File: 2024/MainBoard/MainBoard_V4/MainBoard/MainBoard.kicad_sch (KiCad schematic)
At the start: 15 parts, among them J1 Raspberry_Pi_2_3, SW1 SW_MEC_5E, U1 STM32F446RETx, Y1 CSTNE16M0V530000R0

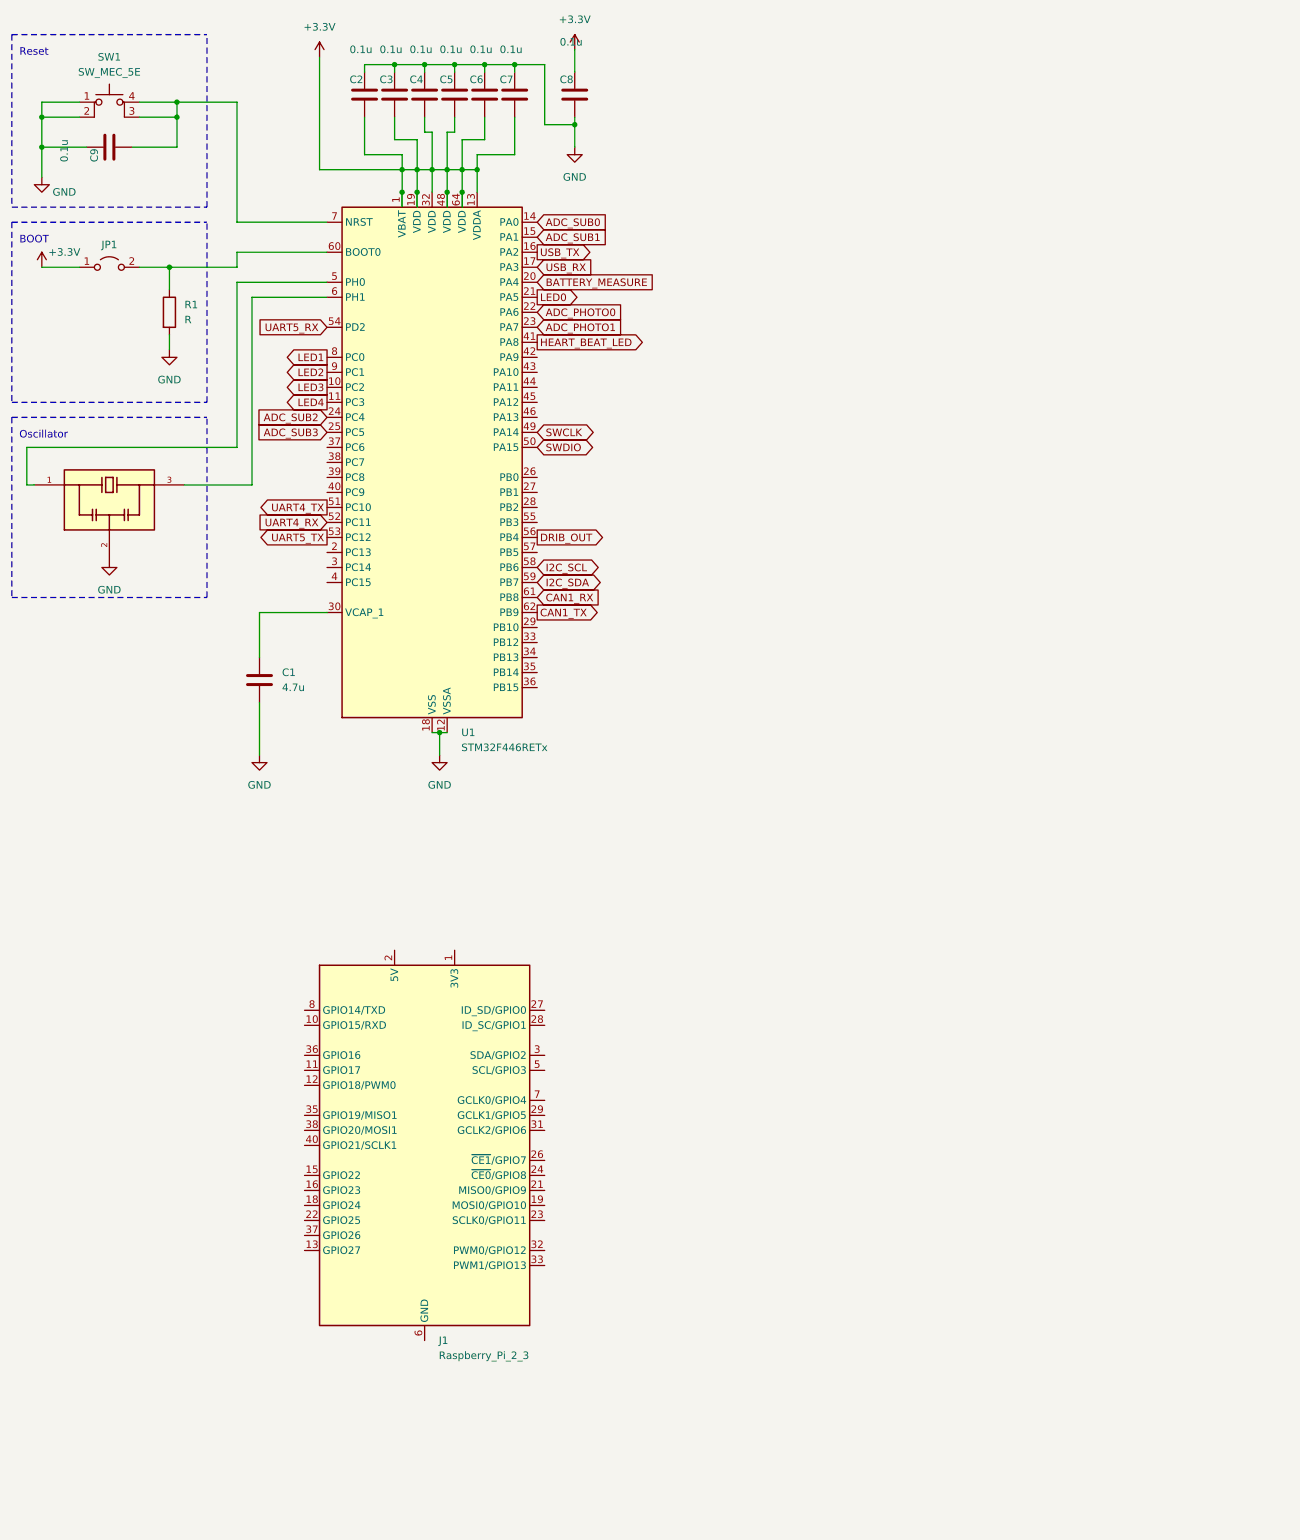
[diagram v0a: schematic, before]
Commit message: ✨ラズパイ周りとUSBシリアル変換周りの回路図を描いた
 USBを刺した時にラズパイが5Vで起動しないようにしないといけない?
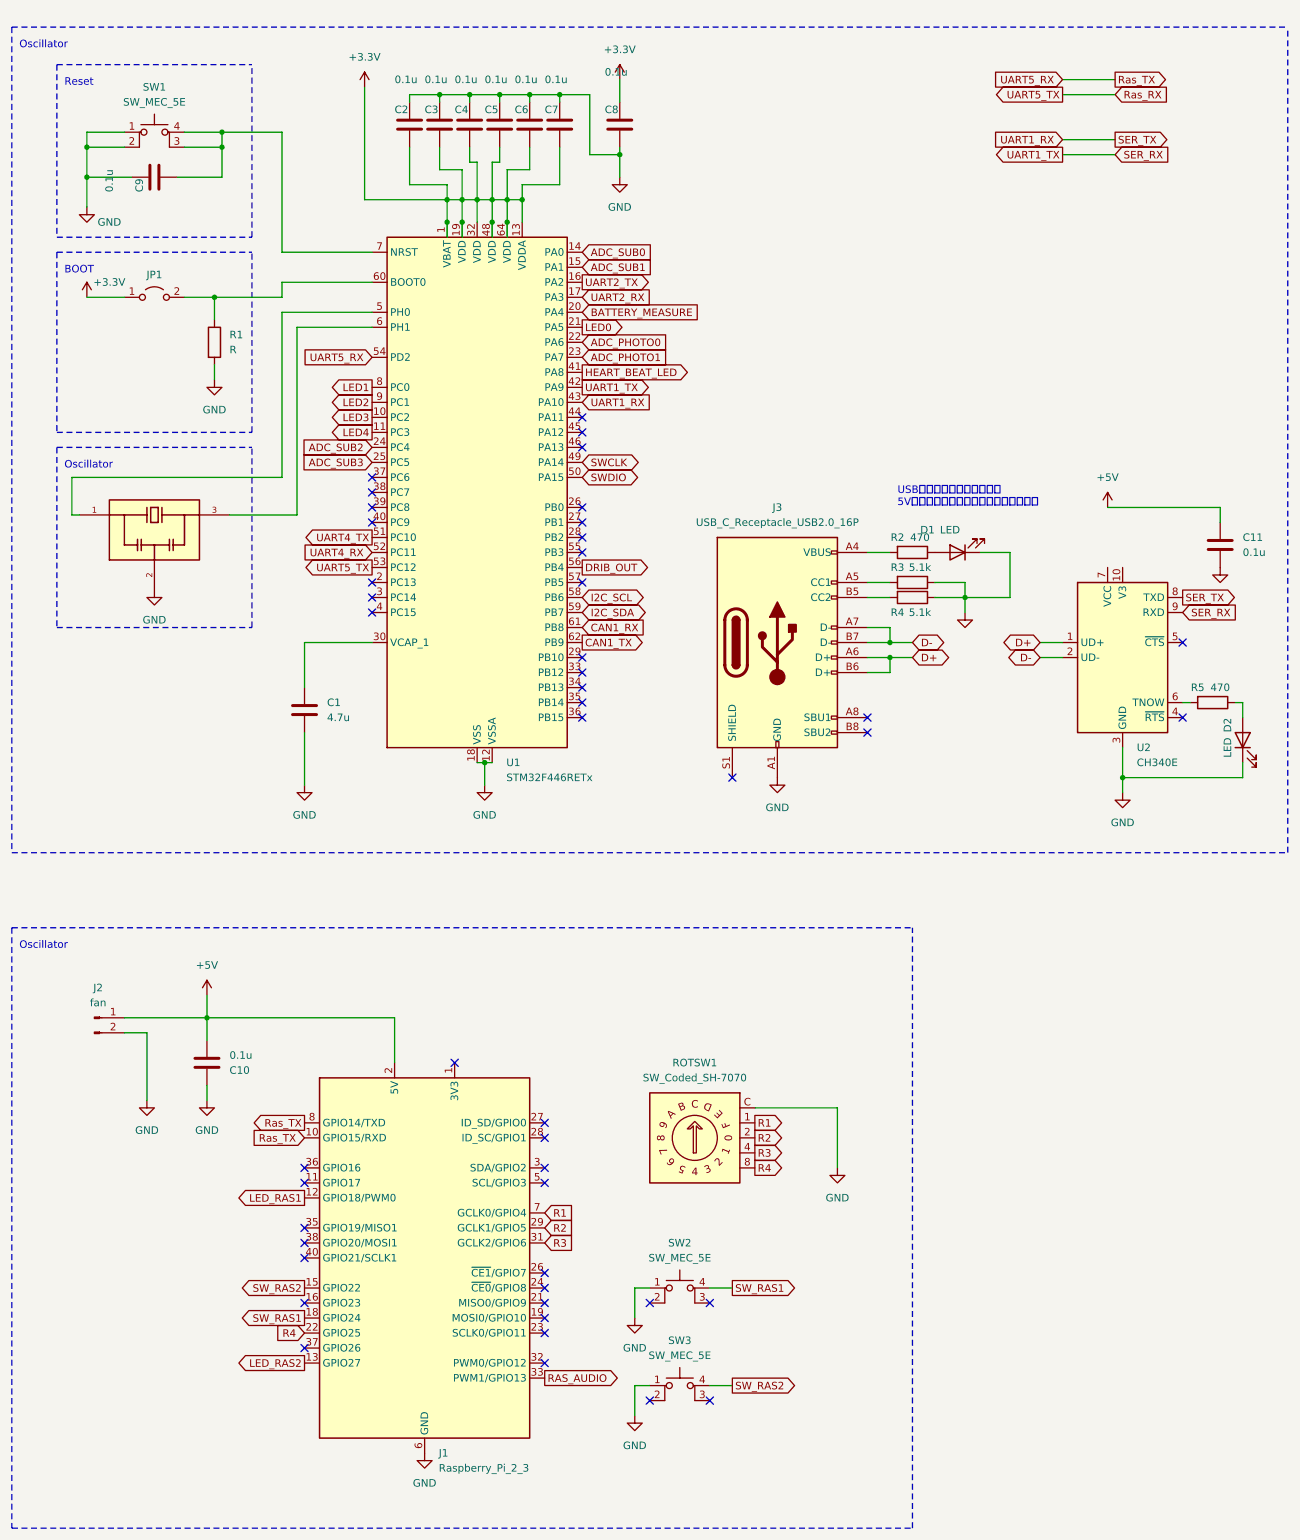
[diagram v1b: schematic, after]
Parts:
- added C10, C11: 0.1u, Capacitor_SMD:C_0504_1310Metric_Pad0.83x1.28mm_HandSolder, symbol Device:C
- added D1, D2: LED, LED_SMD:LED_0603_1608Metric_Pad1.05x0.95mm_HandSolder, symbol Device:LED
- added J2: fan, Resistor_SMD:R_2816_7142Metric_Pad3.20x4.45mm_HandSolder, symbol Connector:Conn_01x02_Pin
- added J3: USB_C_Receptacle_USB2.0_16P, Connector_USB:USB_C_Receptacle_GCT_USB4105-xx-A_16P_TopMnt_Horizontal, symbol Connector:USB_C_Receptacle_USB2.0_16P
- added R2, R5: 470, Resistor_SMD:R_0603_1608Metric_Pad0.98x0.95mm_HandSolder, symbol Device:R
- added R3, R4: 5.1k, Resistor_SMD:R_0603_1608Metric_Pad0.98x0.95mm_HandSolder, symbol Device:R
- added ROTSW1: SW_Coded_SH-7070, symbol Switch:SW_Coded_SH-7070
- added SW2, SW3: SW_MEC_5E, Button_Switch_THT:SW_PUSH_6mm, symbol Switch:SW_MEC_5E
- added U2: CH340E, Package_SO:MSOP-10_3x3mm_P0.5mm, symbol Interface_USB:CH340E
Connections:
- net UART5_RX is gone; now on net Ras_TX: U1.54 (PD2)
- net GND: now also J1.14 (GND), J1.20 (GND), J1.25 (GND), J1.30 (GND), J1.34 (GND), J1.39 (GND), J1.6 (GND), J1.9 (GND), C10.2, C11.2, D1.1 (K), D2.1 (K), J2.2 (Pin_2), J3.A1 (GND), J3.A12 (GND), J3.B1 (GND), J3.B12 (GND), R3.1, R4.1, ROTSW1.C, SW2.1, SW3.1, U2.3 (GND)
- net Ras_TX: now reaches J1.10 (GPIO15/RXD)
- net Ras_TX: now also J1.8 (GPIO14/TXD)
- net LED_RAS1: now reaches J1.12 (GPIO18/PWM0)
- net LED_RAS2: now reaches J1.13 (GPIO27)
- net SW_RAS2: now reaches J1.15 (GPIO22)
- net SW_RAS2: now also SW3.4 (A)
- net SW_RAS1: now reaches J1.18 (GPIO24)
- net SW_RAS1: now also SW2.4 (A)
- net +5V: now reaches J1.2 (5V), J1.4 (5V)
- net +5V: now also C10.1, C11.1, J2.1 (Pin_1)
- net R4: now reaches J1.22 (GPIO25)
- net R4: now also ROTSW1.8
- net R2: now reaches J1.29 (GCLK1/GPIO5)
- net R2: now also ROTSW1.2
- net R3: now reaches J1.31 (GCLK2/GPIO6)
- net R3: now also ROTSW1.4
- net RAS_AUDIO: now reaches J1.33 (PWM1/GPIO13)
- net R1: now reaches J1.7 (GCLK0/GPIO4)
- net R1: now also ROTSW1.1
- net SER_RX: now reaches U1.42 (PA9)
- net SER_RX: now also U2.9 (RXD)
- net SER_TX: now reaches U1.43 (PA10)
- net SER_TX: now also U2.8 (TXD)
- net UART5_TX renamed Ras_RX
- net USB_RX renamed UART2_RX
- net USB_TX renamed UART2_TX
- new net: J3.B5 (CC2), R4.2
- new net: J3.A5 (CC1), R3.2
- new net: R5.2, U2.6 (TNOW)
- new net: D2.2 (A), R5.1
- new net: D1.2 (A), R2.1
- new net: J3.A4 (VBUS), J3.A9 (VBUS), J3.B4 (VBUS), J3.B9 (VBUS), R2.2
- new net D+: J3.A6 (D+), J3.B6 (D+), U2.1 (UD+)
- new net D-: J3.A7 (D-), J3.B7 (D-), U2.2 (UD-)
- no-connect marks 0 -> 47
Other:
- note added: "USBを刺した時にラズパイが 5Vで起動しないようにしないといけない"
- moved on the sheet: C1, C2, C3, C4, C5, C6, C7, C8, C9, J1, JP1, R1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

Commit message: 機能モリモリ基板
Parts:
- removed JP1: Jumper_2_Open, Connector_PinHeader_2.54mm:PinHeader_1x02_P2.54mm_Vertical, symbol Jumper:Jumper_2_Open
- added C12: 0.1u, symbol Device:C
- added C13, C16: 0.1u, Capacitor_SMD:C_0504_1310Metric_Pad0.83x1.28mm_HandSolder, symbol Device:C
- added C14, C15: C, symbol Device:C
- added D10, D11, D12, D13, D14, D15, D3, D7, D8, D9: LED, symbol Device:LED
- added D4, D6: 1N4148W, Diode_SMD:D_SOD-123, symbol Diode:1N4148W
- added D5: 1N4148, Diode_THT:D_DO-35_SOD27_P7.62mm_Horizontal, symbol Diode:1N4148
- added J10: ADC3, symbol Connector:Conn_01x03_Socket
- added J11, J12, J9: ADC2, symbol Connector:Conn_01x03_Socket
- added J13: Drib, symbol Connector:Conn_01x02_Socket
- added J14: UART, symbol Connector:Conn_01x04_Socket
- added J15: TFT3, symbol Connector:Conn_01x04_Socket
- added J4: ST_debug, symbol Connector:Conn_01x07_Socket
- added J5: MOLEX MINISPOX, Connector_Molex:Molex_SPOX_5267-06A_1x06_P2.50mm_Vertical, symbol Connector:Conn_01x06_Socket
- added J6: can_debug, symbol Connector:Conn_01x03_Socket
- added J7: ADC0, symbol Connector:Conn_01x03_Socket
- added J8: ADC1, symbol Connector:Conn_01x03_Socket
- added LS1: PKLCS1212E4001-R1, PKLCS1212E4001-R1:SPKR_PKLCS1212E4001-R1, symbol MainBoard:PKLCS1212E4001-R1
- added Q1: NMOS, symbol Simulation_SPICE:NMOS
- added R10: 4.7k, symbol Device:R
- added R11, R7: 1k, symbol Device:R
- added R12, R13, R14, R15, R16, R17, R18, R19, R21: 300, symbol Device:R
- added R20: 120, Resistor_SMD:R_0603_1608Metric_Pad0.98x0.95mm_HandSolder, symbol Device:R
- added R6: 470, symbol Device:R
- added R8, R9: 2.2k, symbol Device:R
- added SW4: SW_Wuerth_450301014042, Button_Switch_THT:SW_Slide-03_Wuerth-WS-SLTV_10x2.5x6.4_P2.54mm, symbol Switch:SW_Wuerth_450301014042
- added U3: MOUDLE-SEEEDUINO-XIAO, symbol MainBoard:MOUDLE-SEEEDUINO-XIAO
- added U4: ~, symbol MainBoard:TFT1
- added U5: ~, symbol MainBoard:TFT2
- added U6: ~, symbol MainBoard:BNO055
- added U7: AZ1117-3.3, Package_TO_SOT_SMD:SOT-223-3_TabPin2, symbol Regulator_Linear:AZ1117-3.3
- added U8: MAX3051, symbol Interface_UART:MAX3051
- C8: value 0.1u -> 4.7u
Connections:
- net +3.3V: now also C15.1, C16.1, J10.2 (Pin_2), J11.2 (Pin_2), J12.2 (Pin_2), J14.1 (Pin_1), J4.1 (Pin_1), J5.4 (Pin_4), J7.2 (Pin_2), J8.2 (Pin_2), J9.2 (Pin_2), R21.1, SW4.2 (C), U3.12 (3V3), U4.1 (VCC), U7.2 (VO), U8.3 (VDD)
- net +5V: now also U2.7 (VCC), C12.1, C14.1, J5.3 (Pin_3), R6.1, R8.2, R9.2, U3.14 (5V), U6.1 (5V), U7.3 (VI)
- net ADC_PHOTO0: now also J11.1 (Pin_1)
- net ADC_PHOTO1: now also J12.1 (Pin_1)
- net ADC_SUB0: now also J7.1 (Pin_1)
- net ADC_SUB1: now also J8.1 (Pin_1)
- net ADC_SUB2: now also J9.1 (Pin_1)
- net ADC_SUB3: now also J10.1 (Pin_1)
- net BATTERY_MEASURE: now also D6.1 (K)
- net CAN1_RX: now also U8.4 (RXD)
- net CAN1_TX: now also U8.1 (TXD)
- net DRIB_OUT: now also J13.1 (Pin_1)
- net GND: now also C12.2, C13.1, C14.2, C15.2, C16.2, D10.1 (K), D11.1 (K), D12.1 (K), D13.1 (K), D14.1 (K), D15.1 (K), D3.1 (K), D7.1 (K), D8.1 (K), D9.1 (K), J10.3 (Pin_3), J11.3 (Pin_3), J12.3 (Pin_3), J13.2 (Pin_2), J14.2 (Pin_2), J15.1 (Pin_1), J15.2 (Pin_2), J15.3 (Pin_3), J15.4 (Pin_4), J4.3 (Pin_3), J5.1 (Pin_1), J6.3 (Pin_3), J7.3 (Pin_3), J8.3 (Pin_3), J9.3 (Pin_3), Q1.3 (S), R11.2, SW4.3 (A), U3.13 (GND), U4.2 (GND), U6.2 (GND), U7.1 (GND), U8.2 (GND), U8.5 (SHDN), U8.8 (RS)
- net HEART_BEAT_LED: now also R17.1
- net I2C_SCL: now also R9.1, U6.4 (SCL)
- net I2C_SDA: now also R8.1, U6.3 (SDA)
- net LED0: now also R12.1
- net LED1: now also R13.1
- net LED2: now also R14.1
- net LED3: now also R15.1
- net LED4: now also R16.1
- net LED_RAS1: now also R18.1
- net LED_RAS2: now also R19.1
- net RAS_AUDIO: now also D5.2 (A)
- net SER_RX: now also J4.7 (Pin_7)
- net SER_TX: now also J4.6 (Pin_6)
- net SWCLK: now also J4.2 (Pin_2)
- net SWDIO: now also J4.4 (Pin_4)
- net UART4_RX: now also U3.3 (PA10_A2_D2)
- net UART4_TX: now also U3.4 (PA11_A3_D3)
- net NRST: now reaches C9.2, SW1.3 (K), SW1.4 (A), U1.7 (NRST)
- net NRST: now also J4.5 (Pin_5)
- net at R1.1, U1.60 (BOOT0): now also SW4.1 (B)
- net at U2.10 (V3): now also C13.2
- net UART2_RX renamed Port_TX
- net Port_TX: now also J14.3 (Pin_3)
- net UART2_TX renamed Port_RX
- net Port_RX: now also J14.4 (Pin_4)
- new net: D6.2 (A), R10.2, R11.1
- new net: D10.2 (A), R15.2
- new net: LS1.N, Q1.1 (D), R7.2
- new net: D4.1 (K), D5.1 (K), Q1.2 (G)
- new net: D3.2 (A), R6.2
- new net: D11.2 (A), R16.2
- new net: D9.2 (A), R14.2
- new net: D7.2 (A), R12.2
- new net: D12.2 (A), R17.2
- new net: D8.2 (A), R13.2
- new net: D14.2 (A), R19.2
- new net: D13.2 (A), R18.2
- new net: D15.2 (A), R21.2
- new net CANH: J5.5 (Pin_5), J6.1 (Pin_1), R20.1, U8.7 (CANH)
- new net CANL: J5.6 (Pin_6), J6.2 (Pin_2), R20.2, U8.6 (CANL)
- new net D/C: U3.2 (PA4_A1_D1), U4.5 (D/C)
- new net LCD_LED: U3.7 (PB08_A6_D6_TX), U4.8 (LED)
- new net LED_CS: U3.8 (PB09_A7_D7_RX), U4.3 (CS)
- new net MISO: U3.10 (PA5_A9_D9_MISO), U5.4 (T_DOUT)
- new net MOSI: U3.11 (PA6_A10_D10_MOSI), U4.6 (MOSI), U5.3 (T_DIN)
- new net Reset: U3.1 (PA02_A0_D0), U4.4 (Reset)
- new net SCK: U3.9 (PA7_A8_D8_SCK), U4.7 (SCK), U5.1 (T_CLK)
- new net T_CS: U3.5 (PA8_A4_D4_SDA), U5.2 (T_CS)
- new net UI_Audio: D4.2 (A), U3.6 (PA9_A5_D5_SCL)
- new net VD: J5.2 (Pin_2), LS1.P, R10.1, R7.1
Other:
- note added: "Rasberry Pi"
- note added: "STM32F446RE"
- note added: "UI"
- moved on the sheet: D1, R1

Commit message: ✨USB 5Vまわりの修正・綺麗に整理した
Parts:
- removed J4: ST_debug, symbol Connector:Conn_01x07_Socket
- removed J6: can_debug, symbol Connector:Conn_01x03_Socket
- added C17, C18: 0.1u, Capacitor_SMD:C_0603_1608Metric_Pad1.08x0.95mm_HandSolder, symbol Device:C
- added J16, J4: CAN_CON, Connector_JST:JST_PH_S2B-PH-K_1x02_P2.00mm_Horizontal, symbol Connector:Conn_01x02_Socket
- added J6: Debug, Connector_PinHeader_2.54mm:PinHeader_1x07_P2.54mm_Vertical, symbol Connector:Conn_01x07_Pin
- added Q2, Q3: PMOS, symbol Simulation_SPICE:PMOS
- added R22: 1k, Resistor_SMD:R_0603_1608Metric_Pad0.98x0.95mm_HandSolder, symbol Device:R
- added R23: 10K, Resistor_SMD:R_0603_1608Metric_Pad0.98x0.95mm_HandSolder, symbol Device:R
- C1, C10, C11, C13, C16, C2, C3, C4, C5, C6, C7, C8, C9: footprint Capacitor_SMD:C_0504_1310Metric_Pad0.83x1.28mm_HandSolder -> Capacitor_SMD:C_0603_1608Metric_Pad1.08x0.95mm_HandSolder
- C12: footprint (none) -> Capacitor_SMD:C_0603_1608Metric_Pad1.08x0.95mm_HandSolder
- C14, C15: value C -> 1u; footprint (none) -> Capacitor_SMD:C_0603_1608Metric_Pad1.08x0.95mm_HandSolder
- D10, D11, D12, D13, D14, D15, D3, D7, D8, D9: footprint (none) -> LED_SMD:LED_0603_1608Metric_Pad1.05x0.95mm_HandSolder
- J10, J11, J12, J7, J8, J9: footprint (none) -> Connector_JST:JST_XH_S3B-XH-A_1x03_P2.50mm_Horizontal
- J13: footprint (none) -> Connector_JST:JST_XH_S2B-XH-A_1x02_P2.50mm_Horizontal
- J14: footprint (none) -> Connector_JST:JST_XH_S4B-XH-A_1x04_P2.50mm_Horizontal
- J15, U6: footprint (none) -> Connector_PinHeader_2.54mm:PinHeader_1x04_P2.54mm_Vertical
- Q1: footprint (none) -> MainBoard:SOT95P240X111-3N
- R1: value R -> 10k
- R10, R11, R7, R8, R9: footprint (none) -> Resistor_SMD:R_0603_1608Metric_Pad0.98x0.95mm_HandSolder
- R12, R13, R14, R15, R16, R17, R18, R19, R21: value 300 -> 1k; footprint (none) -> Resistor_SMD:R_0603_1608Metric_Pad0.98x0.95mm_HandSolder
- R2: value 470 -> 1k
- R6: value 470 -> 1k; footprint (none) -> Resistor_SMD:R_0603_1608Metric_Pad0.98x0.95mm_HandSolder
- U3: footprint (none) -> MainBoard:MOUDLE14P-SMD-2.54-21X17.8MM
- U4: footprint (none) -> Connector_PinHeader_2.54mm:PinHeader_1x08_P2.54mm_Vertical
- U5: footprint (none) -> Connector_PinHeader_2.54mm:PinHeader_1x05_P2.54mm_Vertical
- U8: footprint (none) -> Package_SO:SOIC-8_3.9x4.9mm_P1.27mm
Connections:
- net +3.3V: now also C17.1
- net +5V: now also C18.1, Q2.3 (S), R22.2; no longer C11.1, C14.1, U2.7 (VCC), U7.3 (VI)
- net CANH: now also J16.1 (Pin_1), J4.1 (Pin_1)
- net CANL: now also J16.2 (Pin_2), J4.2 (Pin_2)
- net GND: now also C17.2, J6.7 (Pin_7), R23.1
- net NRST: now also J6.3 (Pin_3)
- net SWCLK: now also J6.4 (Pin_4)
- net SWDIO: now also J6.5 (Pin_5)
- net +5VL: now reaches J3.A4 (VBUS), J3.A9 (VBUS), J3.B4 (VBUS), J3.B9 (VBUS), R2.2
- net +5VL: now also C11.1, C14.1, U2.7 (VCC), U7.3 (VI), Q3.3 (S)
- net SER_RX renamed UART1_TX
- net SER_TX renamed UART1_RX
- new net: Q2.1 (D), Q3.1 (D)
- new net: C18.2, Q2.2 (G), Q3.2 (G), R22.1, R23.2
- new net UART_RX: J6.1 (Pin_1)
- new net UART_TX: J6.2 (Pin_2)
- new net VDD: J6.6 (Pin_6)
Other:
- note added: "5V(High Current)"
- note added: "Back to Back"
- note added: "Battery Sense"
- note added: "CAN"
- note added: "Connectors"
- note added: "For Low Current Logic"
- note added: "IMU"
- note added: "LEDs"
- note added: "PIEZO"
- note added: "STLink"
- note removed: "USBを刺した時にラズパイが 5Vで起動しないようにしないといけない"
- company: (none) -> Ri-one SSL
- title: (none) -> Main Board V4.0
- moved on the sheet: C10, C11, C12, C13, C14, C15, C16, D1, D10, D11, D12, D13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

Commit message: ✨DXFをインポートした
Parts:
- added H1, H2, H3, H4, H5, H6: MountingHole_Pad, MountingHole:MountingHole_3.2mm_M3_Pad_Via, symbol Mechanical:MountingHole_Pad
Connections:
- net GND: now also H1.1, H2.1, H3.1, H4.1, H5.1, H6.1

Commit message: 部品をおいた
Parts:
- J10, J11, J12, J7, J8, J9: footprint Connector_JST:JST_XH_S3B-XH-A_1x03_P2.50mm_Horizontal -> Connector_JST:JST_PH_B3B-PH-K_1x03_P2.00mm_Vertical
- LS1: footprint PKLCS1212E4001-R1:SPKR_PKLCS1212E4001-R1 -> MainBoard:SPKR_PKLCS1212E4001-R1
- ROTSW1: footprint (none) -> Button_Switch_THT:Nidec_Copal_SH-7010C
- U5: footprint Connector_PinHeader_2.54mm:PinHeader_1x05_P2.54mm_Vertical -> Connector_PinHeader_2.54mm:PinHeader_1x04_P2.54mm_Vertical
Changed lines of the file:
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@@
       (effects (font (size 1.27 1.27)))
     )
-    (property "Footprint" "Connector_PinHeader_2.54mm:PinHeader_1x05_P2.54mm_Vertical" (at 222.25 240.03 0)
+    (property "Footprint" "Connector_PinHeader_2.54mm:PinHeader_1x04_P2.54mm_Vertical" (at 222.25 240.03 0)
       (effects (font (size 1.27 1.27)) hide)
     )
@@
       (effects (font (size 1.27 1.27)) (justify left) hide)
     )
-    (property "Footprint" "PKLCS1212E4001-R1:SPKR_PKLCS1212E4001-R1" (at 398.78 52.07 0)
+    (property "Footprint" "MainBoard:SPKR_PKLCS1212E4001-R1" (at 398.78 52.07 0)
       (effects (font (size 1.27 1.27)) (justify bottom) hide)
     )
@@
       (effects (font (size 1.27 1.27)) (justify left))
     )
-    (property "Footprint" "Connector_JST:JST_XH_S3B-XH-A_1x03_P2.50mm_Horizontal" (at 483.87 119.38 0)
+    (property "Footprint" "Connector_JST:JST_PH_B3B-PH-K_1x03_P2.00mm_Vertical" (at 483.87 119.38 0)
       (effects (font (size 1.27 1.27)) hide)
     )
@@
       (effects (font (size 1.27 1.27)) (justify left))
     )
-    (property "Footprint" "Connector_JST:JST_XH_S3B-XH-A_1x03_P2.50mm_Horizontal" (at 483.87 99.06 0)
+    (property "Footprint" "Connector_JST:JST_PH_B3B-PH-K_1x03_P2.00mm_Vertical" (at 483.87 99.06 0)
       (effects (font (size 1.27 1.27)) hide)
     )
@@
       (effects (font (size 1.27 1.27)) (justify left))
     )
-    (property "Footprint" "Connector_JST:JST_XH_S3B-XH-A_1x03_P2.50mm_Horizontal" (at 514.35 119.38 0)
+    (property "Footprint" "Connector_JST:JST_PH_B3B-PH-K_1x03_P2.00mm_Vertical" (at 514.35 119.38 0)
       (effects (font (size 1.27 1.27)) hide)
     )
@@
       (effects (font (size 1.27 1.27)) (justify left))
     )
-    (property "Footprint" "Connector_JST:JST_XH_S3B-XH-A_1x03_P2.50mm_Horizontal" (at 483.87 78.74 0)
+    (property "Footprint" "Connector_JST:JST_PH_B3B-PH-K_1x03_P2.00mm_Vertical" (at 483.87 78.74 0)
       (effects (font (size 1.27 1.27)) hide)
     )
@@
       (effects (font (size 1.27 1.27)))
     )
-    (property "Footprint" "" (at 133.35 237.49 0)
+    (property "Footprint" "Button_Switch_THT:Nidec_Copal_SH-7010C" (at 133.35 237.49 0)
       (effects (font (size 1.27 1.27)) (justify left) hide)
     )
@@
       (effects (font (size 1.27 1.27)) (justify left))
     )
-    (property "Footprint" "Connector_JST:JST_XH_S3B-XH-A_1x03_P2.50mm_Horizontal" (at 514.35 78.74 0)
+    (property "Footprint" "Connector_JST:JST_PH_B3B-PH-K_1x03_P2.00mm_Vertical" (at 514.35 78.74 0)
       (effects (font (size 1.27 1.27)) hide)
     )
@@
       (effects (font (size 1.27 1.27)) (justify left))
     )
-    (property "Footprint" "Connector_JST:JST_XH_S3B-XH-A_1x03_P2.50mm_Horizontal" (at 514.35 99.06 0)
+    (property "Footprint" "Connector_JST:JST_PH_B3B-PH-K_1x03_P2.00mm_Vertical" (at 514.35 99.06 0)
       (effects (font (size 1.27 1.27)) hide)
     )
